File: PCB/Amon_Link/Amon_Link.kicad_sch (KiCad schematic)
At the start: 100 parts, among them IC1 SPX5205M5-L/TR, J1 USB_C_Receptacle_USB2.0, J2 SMA Edge, J3 Programing port, J4 SMA Edge, SW1 SW_SPST, U1 CH32V003F4P6, U2 CH340G, U3 NRF24L01, U4 RFX2401C, U5 NRF24L01, U6 RFX2401C, Y2 12MHz, Y3 16MHz, Y4 16MHz, Y5 24MHz

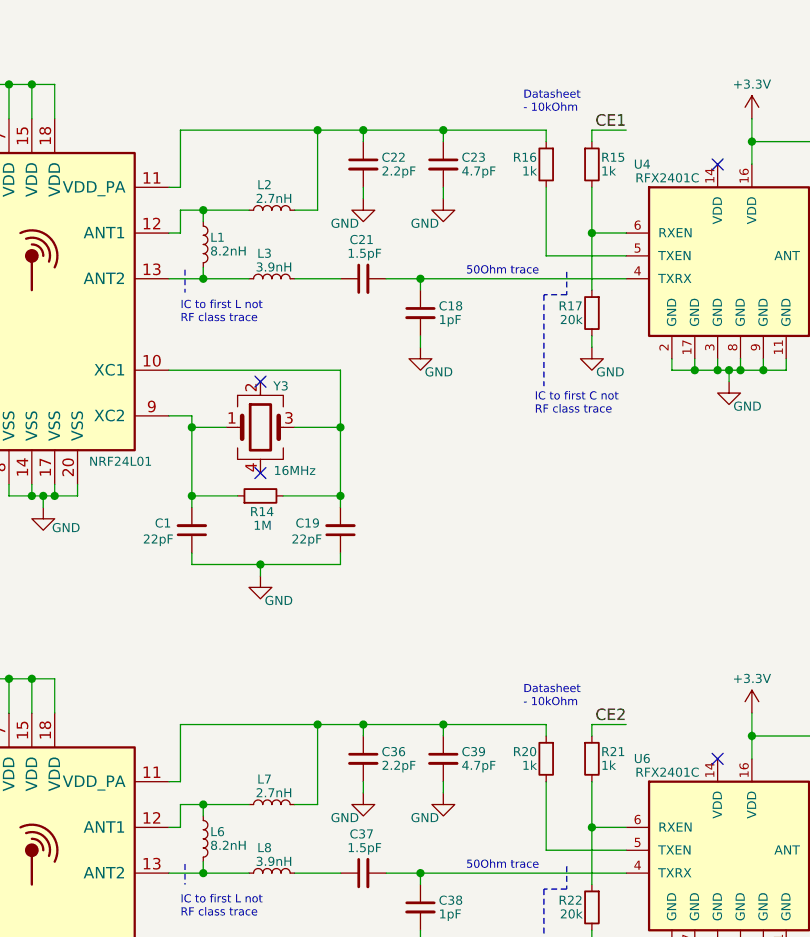
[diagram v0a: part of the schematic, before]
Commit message: Update
nRF25L01 driver complete, untested
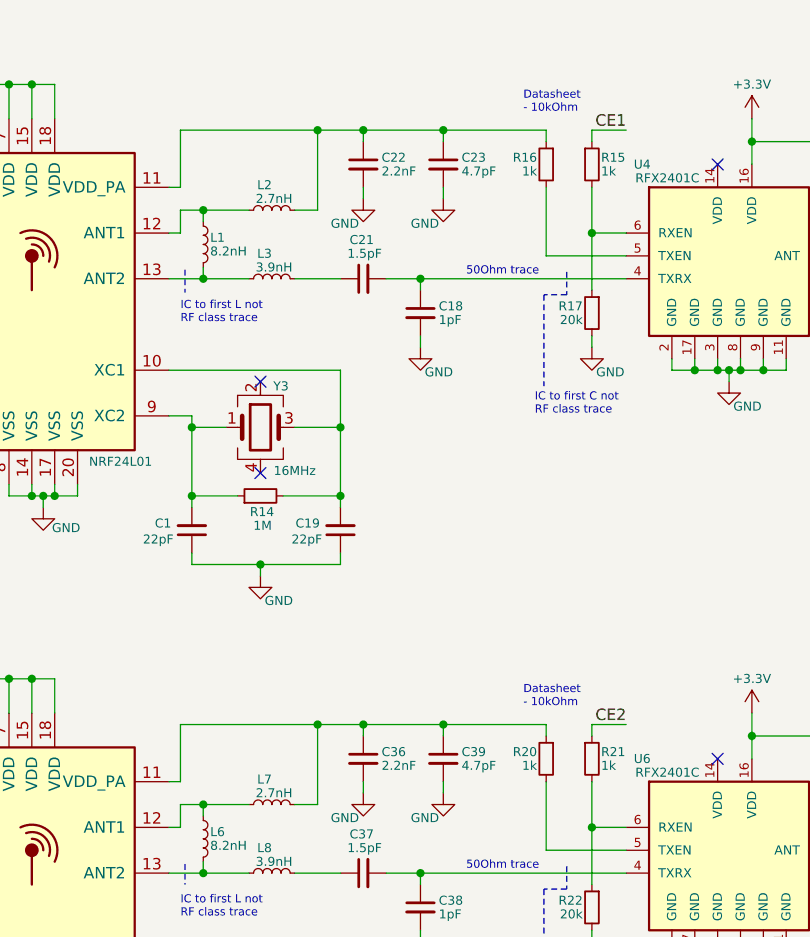
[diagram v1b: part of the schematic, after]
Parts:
- C22, C36: value 2.2pF -> 2.2nF
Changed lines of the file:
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@@
 			)
 		)
-		(property "Value" "2.2pF"
+		(property "Value" "2.2nF"
 			(at 182.372 49.022 0)
 			(effects
@@
 			)
 		)
-		(property "Value" "2.2pF"
+		(property "Value" "2.2nF"
 			(at 182.372 115.062 0)
 			(effects
